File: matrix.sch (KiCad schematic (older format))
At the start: 173 parts

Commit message: Do some routing
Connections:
- net LED: now also R67.2, R70.2; no longer R67.1, R70.1
- net at KBB1.2 (ROW): now also D5.1 (A); no longer D5.2 (A)
- net at KBC1.2 (ROW): now also D5.2 (A); no longer D5.1 (A)
- net at KBD1.2 (ROW): now also D10.1 (A); no longer D10.2 (A)
- net at KBE1.2 (ROW): now also D10.2 (A); no longer D10.1 (A)
- net at KBF1.2 (ROW): now also D14.1 (A); no longer D14.2 (A)
- net at KBG1.2 (ROW): now also D14.2 (A); no longer D14.1 (A)
- net at KBH1.2 (ROW): now also D19.1 (A); no longer D19.2 (A)
- net at KBI1.2 (ROW): now also D20.1 (A); no longer D20.2 (A)
- net at KBJ1.2 (ROW): now also D20.2 (A); no longer D20.1 (A)
- net at KBK1.2 (ROW): now also D24.1 (A); no longer D24.2 (A)
- net at KBL1.2 (ROW): now also D24.2 (A); no longer D24.1 (A)
- net at KBM1.2 (ROW): now also D29.1 (A); no longer D29.2 (A)
- net at KBN1.2 (ROW): now also D29.2 (A); no longer D29.1 (A)
- net at KBO1.2 (ROW): now also D33.1 (A); no longer D33.2 (A)
- net at KBP1-1.2 (ROW), KBP1.2 (ROW): now also D33.2 (A); no longer D33.1 (A)
- net at KBB2.2 (ROW): now also D6.1 (A); no longer D6.2 (A)
- net at KBC2.2 (ROW): now also D6.2 (A); no longer D6.1 (A)
- net at KBD2.2 (ROW): now also D11.1 (A); no longer D11.2 (A)
- net at KBE2.2 (ROW): now also D11.2 (A); no longer D11.1 (A)
- net at KBF2.2 (ROW): now also D15.1 (A); no longer D15.2 (A)
- net at KBG2.2 (ROW): now also D15.2 (A); no longer D15.1 (A)
- net at KBI2.2 (ROW): now also D21.1 (A); no longer D21.2 (A)
- net at KBJ2.2 (ROW): now also D21.2 (A); no longer D21.1 (A)
- net at KBK2.2 (ROW): now also D25.1 (A); no longer D25.2 (A)
- net at KBL2.2 (ROW): now also D25.2 (A); no longer D25.1 (A)
- net at KBM2.2 (ROW): now also D30.1 (A); no longer D30.2 (A)
- net at KBN2.2 (ROW): now also D30.2 (A); no longer D30.1 (A)
- net at KBO2.2 (ROW): now also D34.1 (A); no longer D34.2 (A)
- net at KBP2.2 (ROW): now also D34.2 (A); no longer D34.1 (A)
- net at KBB3-1.2 (ROW), KBB3.2 (ROW): now also D7.1 (A); no longer D7.2 (A)
- net at KBC3.2 (ROW): now also D7.2 (A); no longer D7.1 (A)
- net at KBD3.2 (ROW): now also D12.1 (A); no longer D12.2 (A)
- net at KBE3.2 (ROW): now also D12.2 (A); no longer D12.1 (A)
- net at KBF3.2 (ROW): now also D16.1 (A); no longer D16.2 (A)
- net at KBG3.2 (ROW): now also D16.2 (A); no longer D16.1 (A)
- net at KBI3.2 (ROW): now also D22.1 (A); no longer D22.2 (A)
- net at KBJ3.2 (ROW): now also D22.2 (A); no longer D22.1 (A)
- net at KBK3.2 (ROW): now also D26.1 (A); no longer D26.2 (A)
- net at KBL3.2 (ROW): now also D26.2 (A); no longer D26.1 (A)
- net at KBM3.2 (ROW): now also D31.1 (A); no longer D31.2 (A)
- net at KBN3.2 (ROW): now also D31.2 (A); no longer D31.1 (A)
- net at KBB4.2 (ROW): now also D8.1 (A); no longer D8.2 (A)
- net at KBC4.2 (ROW): now also D8.2 (A); no longer D8.1 (A)
- net at KBD4.2 (ROW): now also D13.1 (A); no longer D13.2 (A)
- net at KBE4.2 (ROW): now also D13.2 (A); no longer D13.1 (A)
- net at KBF4.2 (ROW): now also D17.1 (A); no longer D17.2 (A)
- net at KBG4.2 (ROW): now also D17.2 (A); no longer D17.1 (A)
- net at KBI4.2 (ROW): now also D23.1 (A); no longer D23.2 (A)
- net at KBJ4.2 (ROW): now also D23.2 (A); no longer D23.1 (A)
- net at KBK4.2 (ROW): now also D27.1 (A); no longer D27.2 (A)
- net at KBL4.2 (ROW): now also D27.2 (A); no longer D27.1 (A)
- net at KBM4.2 (ROW): now also D32.1 (A); no longer D32.2 (A)
- net at KBN4.2 (ROW): now also D32.2 (A); no longer D32.1 (A)
- net at KBO4-1.2 (ROW), KBO4.2 (ROW): now also D36.1 (A); no longer D36.2 (A)
- net at KBP4.2 (ROW): now also D36.2 (A); no longer D36.1 (A)
- net at KBP1-1.4 (LEDGND), KBP1.4 (LEDGND): now also R70.1; no longer R70.2
- net at KBO1.4 (LEDGND): now also R67.1; no longer R67.2
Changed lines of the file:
@@
 F 3 "https://assets.nexperia.com/documents/data-sheet/BAV70_SER.pdf" H 2400 7850 50  0001 C CNN
 	1    2400 7850
-	-1   0    0    -1
+	1    0    0    -1
 $EndComp
 Wire Wire Line
@@
 F 3 "https://assets.nexperia.com/documents/data-sheet/BAV70_SER.pdf" H 2400 8800 50  0001 C CNN
 	1    2400 8800
-	-1   0    0    -1
+	1    0    0    -1
 $EndComp
 Wire Wire Line
@@
 F 3 "https://assets.nexperia.com/documents/data-sheet/BAV70_SER.pdf" H 2400 9750 50  0001 C CNN
 	1    2400 9750
-	-1   0    0    -1
+	1    0    0    -1
 $EndComp
 Wire Wire Line
@@
 F 3 "https://assets.nexperia.com/documents/data-sheet/BAV70_SER.pdf" H 3600 9750 50  0001 C CNN
 	1    3600 9750
-	-1   0    0    -1
+	1    0    0    -1
 $EndComp
 Wire Wire Line
@@
 F 3 "https://assets.nexperia.com/documents/data-sheet/BAV70_SER.pdf" H 3600 8800 50  0001 C CNN
 	1    3600 8800
-	-1   0    0    -1
+	1    0    0    -1
 $EndComp
 Wire Wire Line
@@
 F 3 "https://assets.nexperia.com/documents/data-sheet/BAV70_SER.pdf" H 3600 7850 50  0001 C CNN
 	1    3600 7850
-	-1   0    0    -1
+	1    0    0    -1
 $EndComp
 Wire Wire Line
@@
 F 3 "https://assets.nexperia.com/documents/data-sheet/BAV70_SER.pdf" H 4800 7850 50  0001 C CNN
 	1    4800 7850
-	-1   0    0    -1
+	1    0    0    -1
 $EndComp
 Wire Wire Line
@@
 F 3 "https://assets.nexperia.com/documents/data-sheet/BAV70_SER.pdf" H 4800 8800 50  0001 C CNN
 	1    4800 8800
-	-1   0    0    -1
+	1    0    0    -1
 $EndComp
 Wire Wire Line
@@
 F 3 "https://assets.nexperia.com/documents/data-sheet/BAV70_SER.pdf" H 4800 9750 50  0001 C CNN
 	1    4800 9750
-	-1   0    0    -1
+	1    0    0    -1
 $EndComp
 Wire Wire Line
@@
 F 3 "https://assets.nexperia.com/documents/data-sheet/BAV70_SER.pdf" H 6900 6900 50  0001 C CNN
 	1    6900 6900
-	-1   0    0    -1
+	1    0    0    -1
 $EndComp
 Wire Wire Line
@@
 F 3 "https://assets.nexperia.com/documents/data-sheet/BAV70_SER.pdf" H 6900 7850 50  0001 C CNN
 	1    6900 7850
-	-1   0    0    -1
+	1    0    0    -1
 $EndComp
 Wire Wire Line
@@
 F 3 "https://assets.nexperia.com/documents/data-sheet/BAV70_SER.pdf" H 6900 8800 50  0001 C CNN
 	1    6900 8800
-	-1   0    0    -1
+	1    0    0    -1
 $EndComp
 Wire Wire Line
@@
 F 3 "https://assets.nexperia.com/documents/data-sheet/BAV70_SER.pdf" H 6900 9750 50  0001 C CNN
 	1    6900 9750
-	-1   0    0    -1
+	1    0    0    -1
 $EndComp
 Wire Wire Line
@@
 F 3 "https://assets.nexperia.com/documents/data-sheet/BAV70_SER.pdf" H 8100 6900 50  0001 C CNN
 	1    8100 6900
-	-1   0    0    -1
+	1    0    0    -1
 $EndComp
 Wire Wire Line
@@
 F 3 "https://assets.nexperia.com/documents/data-sheet/BAV70_SER.pdf" H 8100 7850 50  0001 C CNN
 	1    8100 7850
-	-1   0    0    -1
+	1    0    0    -1
 $EndComp
 Wire Wire Line
@@
 F 3 "https://assets.nexperia.com/documents/data-sheet/BAV70_SER.pdf" H 8100 8800 50  0001 C CNN
 	1    8100 8800
-	-1   0    0    -1
+	1    0    0    -1
 $EndComp
 Wire Wire Line
@@
 F 3 "https://assets.nexperia.com/documents/data-sheet/BAV70_SER.pdf" H 8100 9750 50  0001 C CNN
 	1    8100 9750
-	-1   0    0    -1
+	1    0    0    -1
 $EndComp
 Wire Wire Line
@@
 F 3 "https://assets.nexperia.com/documents/data-sheet/BAV70_SER.pdf" H 9300 6900 50  0001 C CNN
 	1    9300 6900
-	-1   0    0    -1
+	1    0    0    -1
 $EndComp
 Wire Wire Line
@@
 F 3 "https://assets.nexperia.com/documents/data-sheet/BAV70_SER.pdf" H 9300 7850 50  0001 C CNN
 	1    9300 7850
-	-1   0    0    -1
+	1    0    0    -1
 $EndComp
 Wire Wire Line
@@
 F 3 "https://assets.nexperia.com/documents/data-sheet/BAV70_SER.pdf" H 9300 8800 50  0001 C CNN
 	1    9300 8800
-	-1   0    0    -1
+	1    0    0    -1
 $EndComp
 Wire Wire Line
@@
 F 3 "https://assets.nexperia.com/documents/data-sheet/BAV70_SER.pdf" H 9300 9750 50  0001 C CNN
 	1    9300 9750
-	-1   0    0    -1
+	1    0    0    -1
 $EndComp
 Wire Wire Line
@@
 Wire Wire Line
 	9400 9550 9400 9450
-$Comp
-L keeb_chips:BAV70 D33
-U 1 1 5F591458
-P 10500 6900
-F 0 "D33" H 10500 7116 50  0000 C CNN
-F 1 "BAV70" H 10500 7025 50  0000 C CNN
-F 2 "keeb_parts:SOT-23" H 10500 6900 50  0001 C CNN
-F 3 "https://assets.nexperia.com/documents/data-sheet/BAV70_SER.pdf" H 10500 6900 50  0001 C CNN
-	1    10500 6900
-	-1   0    0    -1
-$EndComp
 Wire Wire Line
 	10400 6600 10400 6700
@@
 F 3 "https://assets.nexperia.com/documents/data-sheet/BAV70_SER.pdf" H 10500 7850 50  0001 C CNN
 	1    10500 7850
-	-1   0    0    -1
+	1    0    0    -1
 $EndComp
 Wire Wire Line
@@
 F 3 "https://assets.nexperia.com/documents/data-sheet/BAV70_SER.pdf" H 10500 9750 50  0001 C CNN
 	1    10500 9750
-	-1   0    0    -1
+	1    0    0    -1
 $EndComp
 Wire Wire Line
@@
 F 3 "~" H 12400 1550 50  0001 C CNN
 	1    12400 1550
-	1    0    0    1
+	-1   0    0    -1
 $EndComp
 Wire Wire Line
@@
 F 3 "~" H 13200 1550 50  0001 C CNN
 	1    13200 1550
-	1    0    0    1
+	-1   0    0    -1
 $EndComp
 Wire Wire Line
@@
 F 3 "https://assets.nexperia.com/documents/data-sheet/BAV70_SER.pdf" H 5900 7000 50  0001 C CNN
 	1    5900 7000
-	-1   0    0    -1
+	1    0    0    -1
 $EndComp
 $Comp
@@
 F 3 "https://assets.nexperia.com/documents/data-sheet/BAV70_SER.pdf" H 4800 6900 50  0001 C CNN
 	1    4800 6900
-	-1   0    0    -1
+	1    0    0    -1
 $EndComp
 $Comp
@@
 F 3 "https://assets.nexperia.com/documents/data-sheet/BAV70_SER.pdf" H 3600 6900 50  0001 C CNN
 	1    3600 6900
-	-1   0    0    -1
+	1    0    0    -1
 $EndComp
 $Comp
@@
 F 3 "https://assets.nexperia.com/documents/data-sheet/BAV70_SER.pdf" H 2400 6900 50  0001 C CNN
 	1    2400 6900
-	-1   0    0    -1
+	1    0    0    -1
 $EndComp
 $Comp
@@
 	-1   0    0    -1
 $EndComp
+$Comp
+L keeb_chips:BAV70 D33
+U 1 1 5F591458
+P 10500 6900
+F 0 "D33" H 10500 7116 50  0000 C CNN
+F 1 "BAV70" H 10500 7025 50  0000 C CNN
+F 2 "keeb_parts:SOT-23" H 10500 6900 50  0001 C CNN
+F 3 "https://assets.nexperia.com/documents/data-sheet/BAV70_SER.pdf" H 10500 6900 50  0001 C CNN
+	1    10500 6900
+	1    0    0    -1
+$EndComp
 $EndSCHEMATC

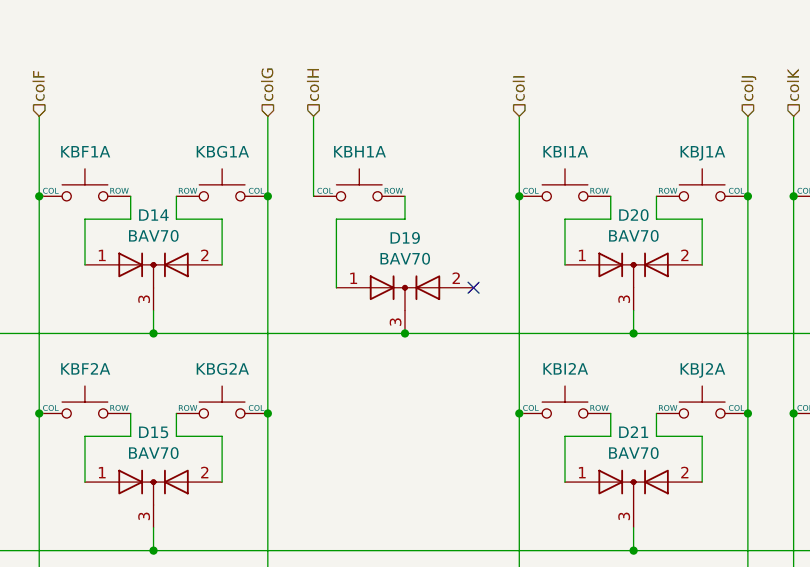
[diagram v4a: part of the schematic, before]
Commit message: Finish routing switches
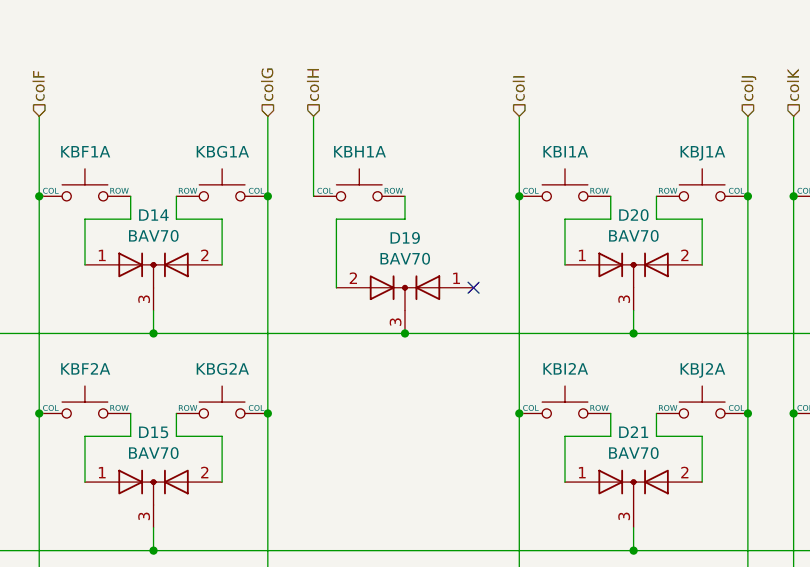
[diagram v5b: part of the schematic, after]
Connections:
- net at KBH1.2 (ROW): now also D19.2 (A); no longer D19.1 (A)
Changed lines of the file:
@@
 F 3 "https://assets.nexperia.com/documents/data-sheet/BAV70_SER.pdf" H 5900 7000 50  0001 C CNN
 	1    5900 7000
-	1    0    0    -1
+	-1   0    0    -1
 $EndComp
 $Comp
